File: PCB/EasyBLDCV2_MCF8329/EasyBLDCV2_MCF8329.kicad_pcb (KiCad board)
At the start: 4 copper layers, 72.4 x 45.7 mm, 79 parts, among them J1 10159560-A00221RLF, J2 FTSH-105-01-F-DV-P-TR, Q1 CSD16556Q5B, Q2 CSD16556Q5B, Q3 CSD16556Q5B, Q4 CSD16556Q5B, Q5 CSD16556Q5B, Q6 CSD16556Q5B, U1 DRV83053PHP, U2 TMS320F28027FPTT, U3 TPD4E05U06DQAR, U4 LMR16006XDDCR

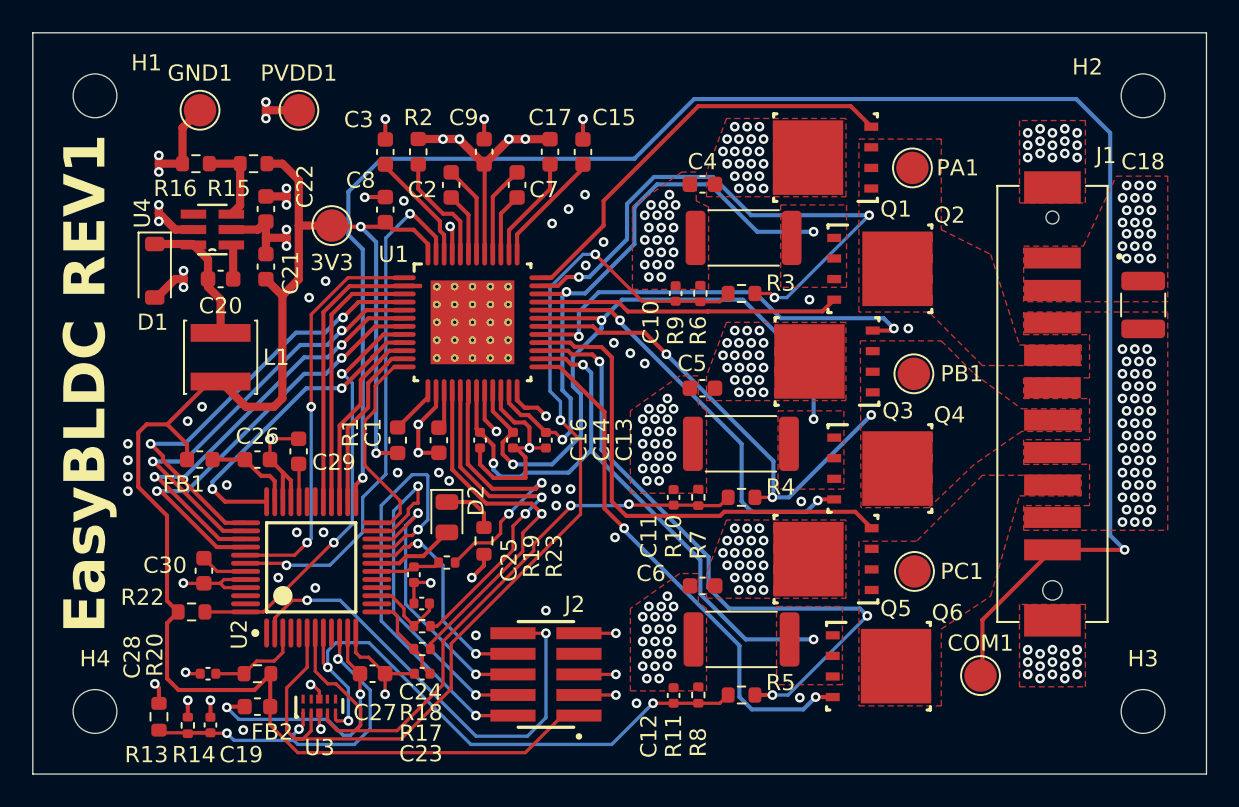
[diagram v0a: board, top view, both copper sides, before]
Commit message: Deleted V1 Relics, redid power stage
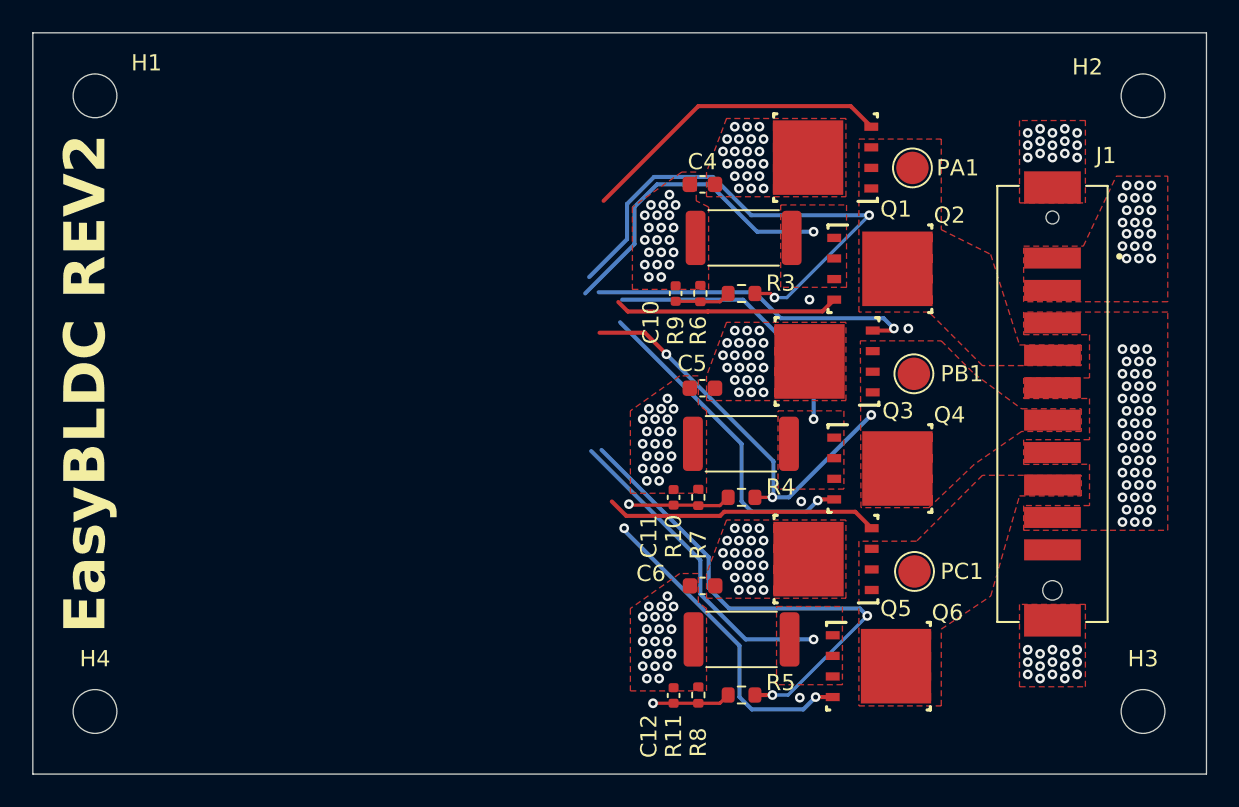
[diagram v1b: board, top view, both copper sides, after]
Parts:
- removed 3V3, COM1, GND1, PVDD1: TestPoint, TestPoint:TestPoint_Pad_D2.0mm
- removed C1, C17, C22, C3, C8: 1u, Capacitor_SMD:C_0603_1608Metric
- removed C13, C14, C16: 1n, Capacitor_SMD:C_0402_1005Metric
- removed C15, C26, C27, C29, C30: 2.2u, Capacitor_SMD:C_0603_1608Metric
- removed C18: 10u, Capacitor_SMD:C_1210_3225Metric
- removed C19, C28: 0.1u, Capacitor_SMD:C_0402_1005Metric
- removed C2, C7: 47n, Capacitor_SMD:C_0603_1608Metric
- removed C20: 0.33u, Capacitor_SMD:C_0603_1608Metric
- removed C21: 22u, Capacitor_SMD:C_0603_1608Metric
- removed C23, C24, C25: 2.2n, Capacitor_SMD:C_0402_1005Metric
- removed C9: 4.7u, Capacitor_SMD:C_0603_1608Metric
- removed D1: D_Schottky, Diode_SMD:D_SOD-123
- removed D2: GREEN, LED_SMD:LED_0805_2012Metric
- removed FB1, FB2: 600, Inductor_SMD:L_0603_1608Metric
- removed J2: FTSH-105-01-F-DV-P-TR, EasyBLDC:SAMTEC_FTSH-105-01-F-DV-P-TR
- removed L1: SD53-120-R, Inductor_SMD:L_Changjiang_FNR4020S
- removed R1: 10K, Fuse:Fuse_0603_1608Metric
- removed R13: 24.9K, Resistor_SMD:R_0603_1608Metric
- removed R14: 4.99K, Resistor_SMD:R_0402_1005Metric
- removed R15: 68k, Resistor_SMD:R_0603_1608Metric
- removed R16: 20k, Resistor_SMD:R_0603_1608Metric
- removed R17, R18, R19: 56, Resistor_SMD:R_0402_1005Metric
- removed R2: 100, Fuse:Fuse_0603_1608Metric
- removed R20: 47K, Resistor_SMD:R_0603_1608Metric
- removed R22: 10K, Resistor_SMD:R_0603_1608Metric
- removed R23: 330, Resistor_SMD:R_0603_1608Metric
- removed U1: DRV83053PHP, EasyBLDC:PHP0048G_N
- removed U2: TMS320F28027FPTT, EasyBLDC:PT0048A_N
- removed U3: TPD4E05U06DQAR, EasyBLDC:DQA0010A
- removed U4: LMR16006XDDCR, EasyBLDC:DDC0006A
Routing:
- net COM: track 110.4 -> 0.00 mm, vias 2 -> 0
- net 3.3V: track 104.0 -> 0.00 mm, vias 2 -> 0
- net GND: track 83.6 -> 0.44 mm, vias 204 -> 142
- net VSEN_A: track 62.6 -> 3.46 mm, vias 2 -> 0
- net VSEN_B: track 41.3 -> 6.50 mm, vias 2 -> 1
- net VSEN_C: track 37.1 -> 4.85 mm, vias 3 -> 1
- net WAKE: track 32.2 -> 0.00 mm, vias 2 -> 0
- net nTRST: track 29.3 -> 0.00 mm, vias 2 -> 0
- net TMS: track 27.9 -> 0.00 mm, vias 2 -> 0
- net INH_B: track 27.3 -> 0.00 mm, vias 2 -> 0
- net INL_B: track 26.9 -> 0.00 mm, vias 2 -> 0
- net INH_C: track 26.6 -> 0.00 mm, vias 2 -> 0
- net INL_C: track 26.4 -> 0.00 mm, vias 2 -> 0
- net nFAULT: track 25.8 -> 0.00 mm, vias 2 -> 0
- net PVDD: track 25.2 -> 0.00 mm, vias 95 -> 84
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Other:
- board text added: "EasyBLDC REV2"
- board text removed: "EasyBLDC REV1"

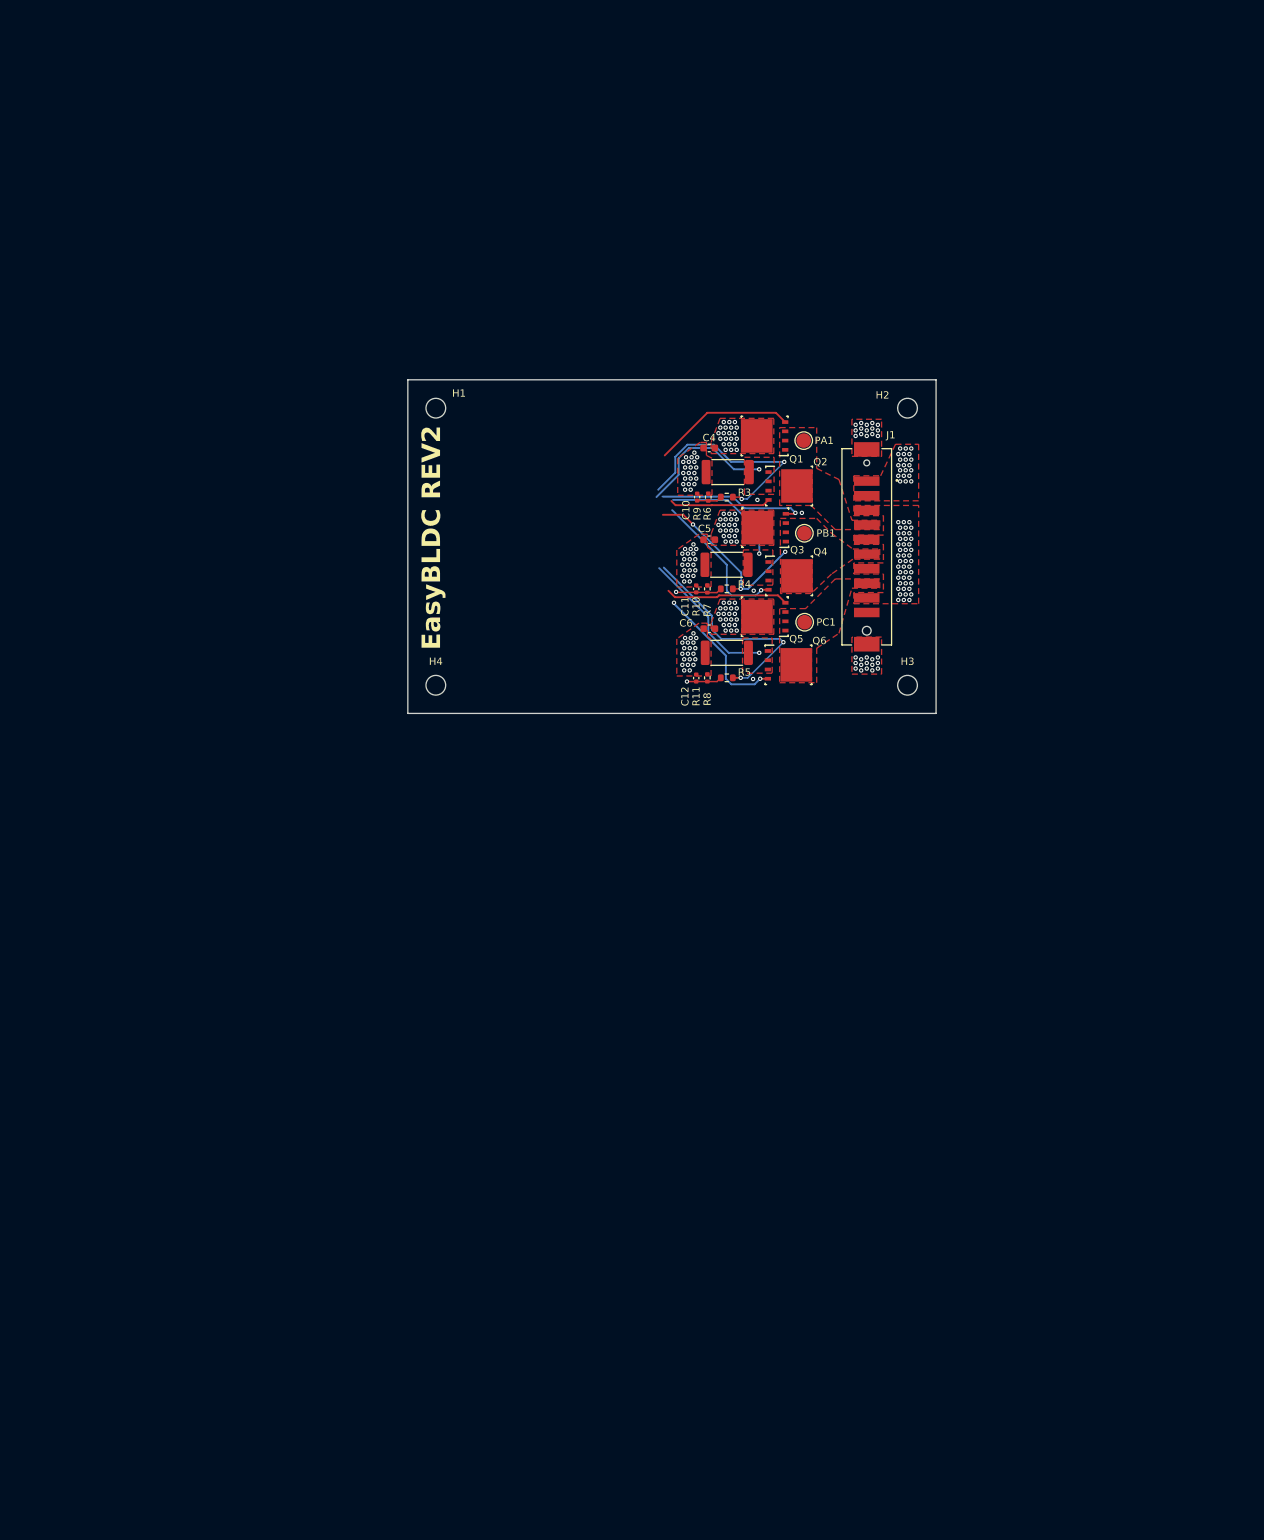
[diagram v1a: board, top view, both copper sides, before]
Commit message: Assigned footprints, created bom
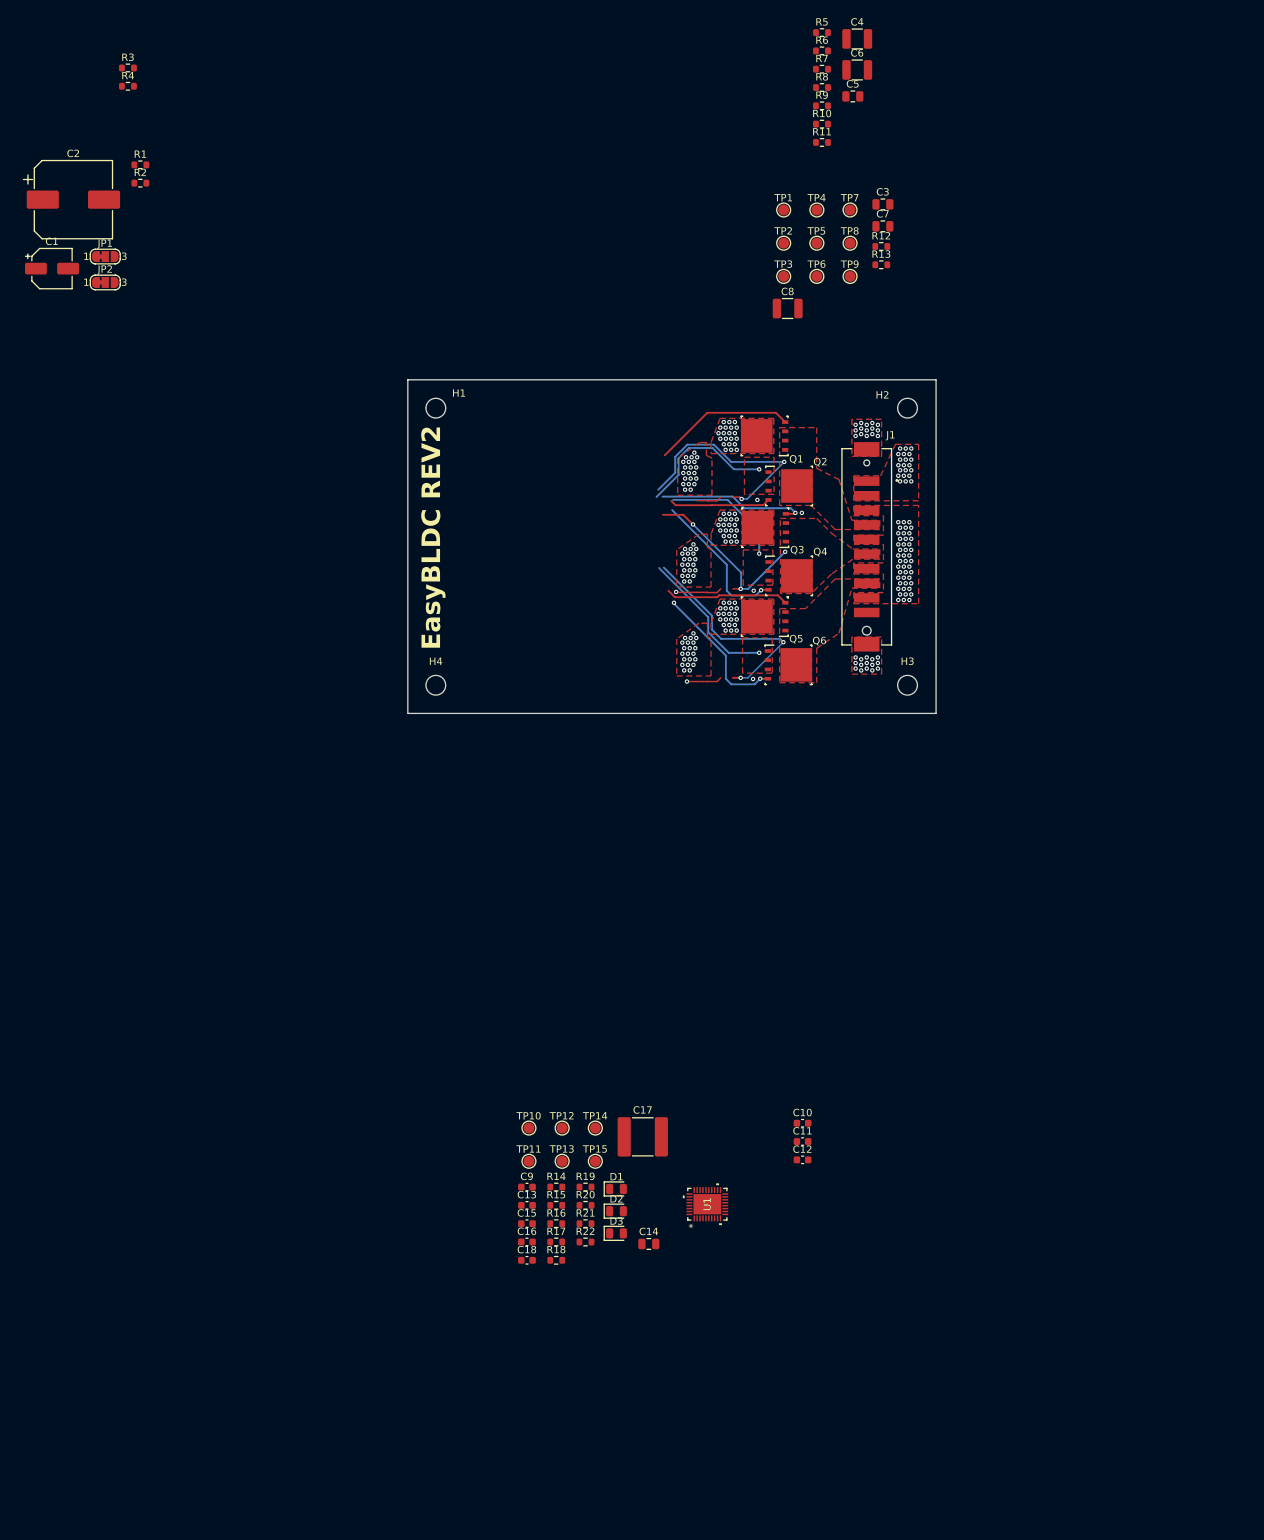
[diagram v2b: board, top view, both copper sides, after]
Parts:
- removed PA1, PB1, PC1: TestPoint, TestPoint:TestPoint_Pad_D2.0mm
- added C1: 10u, Capacitor_SMD:CP_Elec_5x5.3, F.Cu at (-24.5, 13.3)
- added C13: 0.1u, Capacitor_SMD:C_0603_1608Metric, F.Cu at (40.6, 141.6)
- added C14: 470n, Capacitor_SMD:C_0805_2012Metric, F.Cu at (57.3, 146.9)
- added C15: 1u, Capacitor_SMD:C_0603_1608Metric, F.Cu at (40.6, 144.1)
- added C16: 10u, Capacitor_SMD:C_0603_1608Metric, F.Cu at (40.6, 146.7)
- added C17: 10u, Capacitor_SMD:C_2220_5750Metric, F.Cu at (56.4, 132.2)
- added C18: 100n, Capacitor_SMD:C_0603_1608Metric, F.Cu at (40.6, 149.2)
- added C2: 220u, Capacitor_SMD:CP_Elec_10x10.5, F.Cu at (-21.6, 3.81)
- added C3: 0.01u, Capacitor_SMD:C_0805_2012Metric, F.Cu at (89.3, 4.46)
- added C7: 0.01u, Capacitor_SMD:C_0805_2012Metric, F.Cu at (89.3, 7.47)
- added C8: 4.7u, Capacitor_SMD:C_1210_3225Metric, F.Cu at (76.3, 18.7)
- added C9: 1u, Capacitor_SMD:C_0603_1608Metric, F.Cu at (40.6, 139.1)
- added D1: GREEN, LED_SMD:LED_0805_2012Metric, F.Cu at (52.8, 139.4)
- added D2: GREEN, LED_SMD:LED_0805_2012Metric, F.Cu at (52.8, 142.4)
- added D3: RED, LED_SMD:LED_0805_2012Metric, F.Cu at (52.8, 145.5)
- added JP1: SolderJumper_3_Bridged12, Jumper:SolderJumper-3_P1.3mm_Bridged12_RoundedPad1.0x1.5mm_NumberLabels, F.Cu at (-17.2, 11.6)
- added JP2: SolderJumper_3_Bridged12, Jumper:SolderJumper-3_P1.3mm_Bridged12_RoundedPad1.0x1.5mm_NumberLabels, F.Cu at (-17.2, 15.2)
- added R1: 10k, Resistor_SMD:R_0603_1608Metric, F.Cu at (-12.4, -0.96)
- added R12: 0.001, Resistor_SMD:R_0603_1608Metric, F.Cu at (89.1, 10.2)
- added R13: 0, Resistor_SMD:R_0603_1608Metric, F.Cu at (89.1, 12.7)
- added R14: 5.1k, Resistor_SMD:R_0603_1608Metric, F.Cu at (44.6, 139.1)
- added R15: 5.1k, Resistor_SMD:R_0603_1608Metric, F.Cu at (44.6, 141.6)
- added R16: 0, Resistor_SMD:R_0603_1608Metric, F.Cu at (44.6, 144.1)
- added R17: 5.1k, Resistor_SMD:R_0603_1608Metric, F.Cu at (44.6, 146.7)
- added R18: 0, Resistor_SMD:R_0603_1608Metric, F.Cu at (44.6, 149.2)
- added R19: 5.1k, Resistor_SMD:R_0603_1608Metric, F.Cu at (48.6, 139.1)
- added R2: 10k, Resistor_SMD:R_0603_1608Metric, F.Cu at (-12.4, 1.55)
- added R20: 2k, Resistor_SMD:R_0603_1608Metric, F.Cu at (48.6, 141.6)
- added R21: 890, Resistor_SMD:R_0603_1608Metric, F.Cu at (48.6, 144.1)
- added R22: 890, Resistor_SMD:R_0603_1608Metric, F.Cu at (48.6, 146.7)
- added TP1: TestPoint, TestPoint:TestPoint_Pad_D1.5mm, F.Cu at (75.7, 5.23)
- added TP10: TestPoint, TestPoint:TestPoint_Pad_D1.5mm, F.Cu at (40.8, 131.0)
- added TP11: TestPoint, TestPoint:TestPoint_Pad_D1.5mm, F.Cu at (40.8, 135.6)
- added TP12: TestPoint, TestPoint:TestPoint_Pad_D1.5mm, F.Cu at (45.4, 131.0)
- added TP13: TestPoint, TestPoint:TestPoint_Pad_D1.5mm, F.Cu at (45.4, 135.6)
- added TP14: TestPoint, TestPoint:TestPoint_Pad_D1.5mm, F.Cu at (49.9, 131.0)
- added TP15: TestPoint, TestPoint:TestPoint_Pad_D1.5mm, F.Cu at (49.9, 135.6)
- added TP2: TestPoint, TestPoint:TestPoint_Pad_D1.5mm, F.Cu at (75.7, 9.78)
- added TP3: TestPoint, TestPoint:TestPoint_Pad_D1.5mm, F.Cu at (75.7, 14.3)
- added TP4: TestPoint, TestPoint:TestPoint_Pad_D1.5mm, F.Cu at (80.3, 5.23)
- added TP5: TestPoint, TestPoint:TestPoint_Pad_D1.5mm, F.Cu at (80.3, 9.78)
- added TP6: TestPoint, TestPoint:TestPoint_Pad_D1.5mm, F.Cu at (80.3, 14.3)
- added TP7: TestPoint, TestPoint:TestPoint_Pad_D1.5mm, F.Cu at (84.8, 5.23)
- added TP8: TestPoint, TestPoint:TestPoint_Pad_D1.5mm, F.Cu at (84.8, 9.78)
- added TP9: TestPoint, TestPoint:TestPoint_Pad_D1.5mm, F.Cu at (84.8, 14.3)
- added U1: MCF8329A1IREER, EasyBLDC:WQFN36_REE_TEX, F.Cu at (65.3, 141.5)
- C10, C11: value 0.1u -> 1u; footprint Capacitor_SMD:C_0402_1005Metric -> Capacitor_SMD:C_0603_1608Metric
- C12: value 0.1u -> 10u; footprint Capacitor_SMD:C_0402_1005Metric -> Capacitor_SMD:C_0603_1608Metric
- C4, C6: value 1u -> 4.7u; footprint Capacitor_SMD:C_0603_1608Metric -> Capacitor_SMD:C_1210_3225Metric
- C5: value 1u -> 0.01u; footprint Capacitor_SMD:C_0603_1608Metric -> Capacitor_SMD:C_0805_2012Metric
- Q1, Q2, Q3, Q4, Q5, Q6: value CSD16556Q5B -> CSD17573Q5B
- R10, R9: value 4.99K -> 10; footprint Resistor_SMD:R_0402_1005Metric -> Resistor_SMD:R_0603_1608Metric
- R11: value 4.99K -> 0; footprint Resistor_SMD:R_0402_1005Metric -> Resistor_SMD:R_0603_1608Metric
- R3, R4: value 0.007 -> 10k; footprint Resistor_SMD:R_2512_6332Metric -> Resistor_SMD:R_0603_1608Metric
- R5: value 0.007 -> 10; footprint Resistor_SMD:R_2512_6332Metric -> Resistor_SMD:R_0603_1608Metric
- R6, R7, R8: value 24.9K -> 10
- moved R4 105.0 mm to (-14.1, -11.7), turned to 0 degrees
- moved R3 99.1 mm to (-14.1, -14.2), turned to 0 degrees
- moved C10 87.0 mm to (78.3, 130.4), turned to 0 degrees
- moved R5 86.0 mm to (81.0, -19.1), turned to 0 degrees
- moved R8 81.9 mm to (81.0, -11.6), turned to 0 degrees
- moved C6 79.2 mm to (85.8, -14.0), turned to 0 degrees
- moved C11 77.1 mm to (78.3, 132.9), turned to 0 degrees
- moved R11 75.0 mm to (81.0, -4.03), turned to 0 degrees
- moved R7 72.4 mm to (81.0, -14.1), turned to 0 degrees
- moved C12 67.6 mm to (78.3, 135.4), turned to 0 degrees
- moved R10 65.6 mm to (81.0, -6.54), turned to 0 degrees
- moved C5 63.9 mm to (85.2, -10.3), turned to 0 degrees
- moved R6 62.5 mm to (81.0, -16.6), turned to 0 degrees
- moved C4 59.6 mm to (85.8, -18.2), turned to 0 degrees
- moved R9 55.8 mm to (81.0, -9.04), turned to 0 degrees
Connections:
- C10 pad 1: VSEN_A -> Net-(U1A-SHB)
- C10 pad 2: GND -> BSTB
- C11 pad 1: VSEN_B -> Net-(U1A-SHC)
- C11 pad 2: GND -> BSTC
- C12 pad 1: VSEN_C -> AVDD
- C5 pad 2: GND -> LSS
- Q1 pad 4: GH_A -> Net-(Q1-G)
- Q2 pad 1: SL_A -> LSS
- Q2 pad 2: SL_A -> LSS
- Q2 pad 3: SL_A -> LSS
- Q2 pad 4: GL_A -> Net-(Q2-G)
- Q3 pad 4: GH_B -> Net-(Q3-G)
- Q4 pad 1: SL_B -> LSS
- Q4 pad 2: SL_B -> LSS
- Q4 pad 3: SL_B -> LSS
- Q4 pad 4: GL_B -> Net-(Q4-G)
- Q5 pad 4: GH_C -> Net-(Q5-G)
- Q6 pad 1: SL_C -> LSS
- Q6 pad 2: SL_C -> LSS
- Q6 pad 3: SL_C -> LSS
- Q6 pad 4: GL_C -> Net-(Q6-G)
- R10 pad 1: VSEN_B -> GL_C
- R10 pad 2: GND -> Net-(Q6-G)
- R11 pad 1: VSEN_C -> LSS
- R11 pad 2: GND -> SP
- R3 pad 1: SL_A -> GND
- R3 pad 2: GND -> BRAKE
- R4 pad 1: SL_B -> GND
- R4 pad 2: GND -> Net-(JP2-A)
- R5 pad 1: SL_C -> GH_A
- R5 pad 2: GND -> Net-(Q1-G)
- R6 pad 1: MOT_A -> GH_B
- R6 pad 2: VSEN_A -> Net-(Q3-G)
- R7 pad 1: MOT_B -> GH_C
- R7 pad 2: VSEN_B -> Net-(Q5-G)
- R8 pad 1: MOT_C -> GL_A
- R8 pad 2: VSEN_C -> Net-(Q2-G)
- R9 pad 1: VSEN_A -> GL_B
- R9 pad 2: GND -> Net-(Q4-G)
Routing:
- net Net-(Q3-G): track 0.00 -> 20.5 mm, vias 0 -> 1
- net GH_B: track 20.5 -> 0.00 mm, vias 1 -> 0
- net Net-(Q4-G): track 0.00 -> 20.4 mm, vias 0 -> 1
- net GL_B: track 20.4 -> 0.00 mm, vias 1 -> 0
- net SL_C: track 19.8 -> 0.00 mm, vias 1 -> 0
- net Net-(Q6-G): track 0.00 -> 19.6 mm, vias 0 -> 2
- net GL_C: track 19.6 -> 0.00 mm, vias 2 -> 0
- net Net-(Q1-G): track 0.00 -> 19.5 mm
- net SL_A: track 19.4 -> 0.00 mm, vias 1 -> 0
- net GND: track 0.44 -> 19.9 mm, vias 142 -> 143
- net Net-(Q2-G): track 0.00 -> 17.3 mm
- net Net-(Q5-G): track 0.00 -> 16.9 mm
- net GH_C: track 16.9 -> 0.00 mm
- net SL_B: track 16.6 -> 0.00 mm, vias 1 -> 0
- net LSS: track 0.00 -> 16.6 mm, vias 0 -> 1
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- added copper zone on F.Cu, net LSS
- removed copper zone on F.Cu, net SL_A
- removed copper zone on F.Cu, net SL_B
- removed copper zone on F.Cu, net SL_C
